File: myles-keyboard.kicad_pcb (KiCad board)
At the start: 2 copper layers, 208.8 x 114.3 mm, 52 parts, among them J1 TRRS, J2 OLED, SW00 Key, SW01 Key, SW02 Key, SW03 Key, SW04 Key, SW05 Key, SW10 Key, SW11 Key, SW12 Key, SW13 Key, SW14 Key, SW15 Key, SW16 Key, SW17 Key, SW18 Key, SW20 Key, SW21 Key, SW22 Key, SW23 Key, SW24 Key, SW25 Key, SW26 Key, SW27 Key, SW28 Key, SW30 Key, SW31 Key, SW32 Key, SW33 Key, SW34 Key, SW35 Key, SW36 Key, SW37 Key, SW38 Key, SW40 Key, SW41 Key, SW42 Key, SW43 Key, SW44 Key, SW45 Key, SW46 Key, SW47 Key, SW48 Key, U1 ProMicro

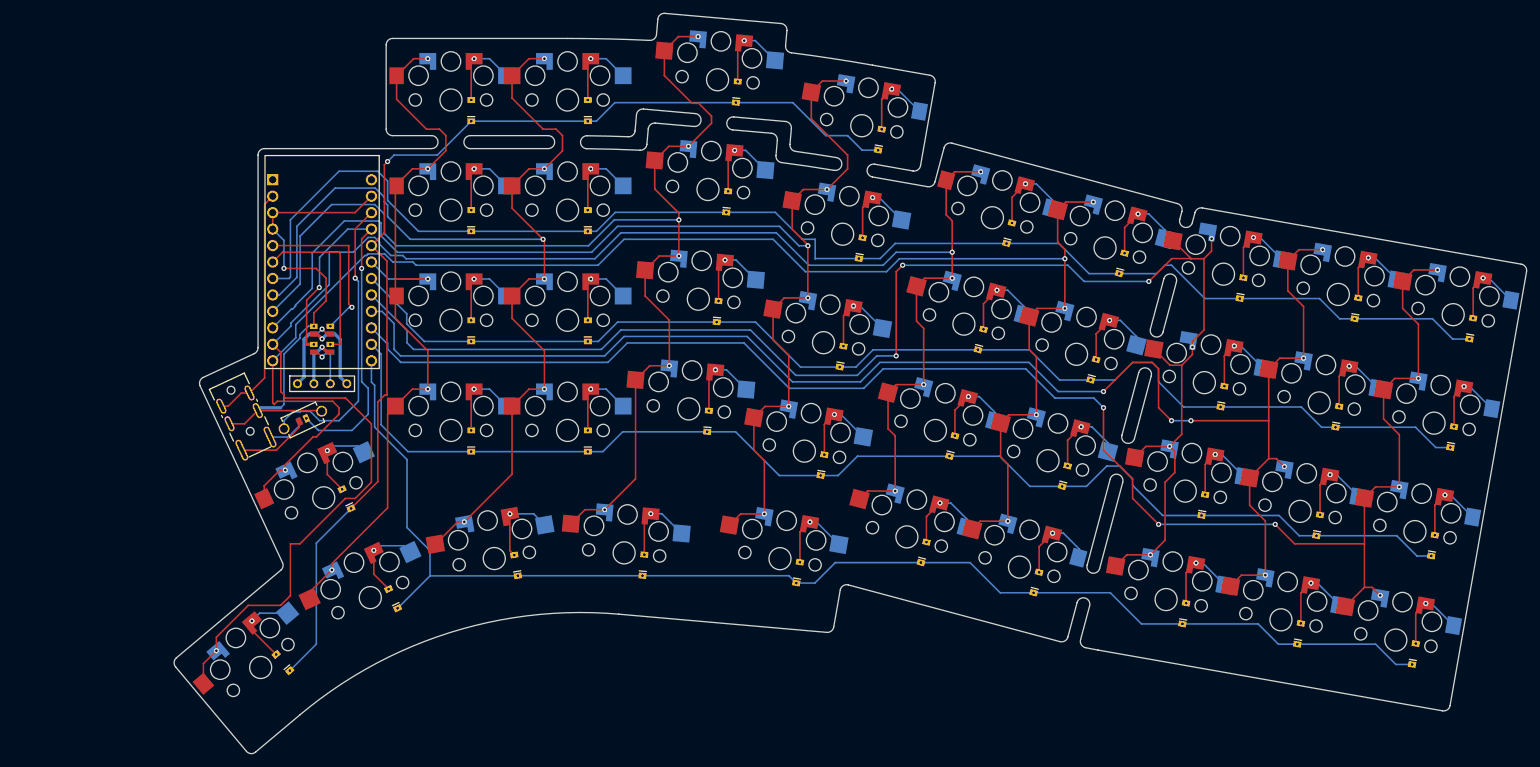
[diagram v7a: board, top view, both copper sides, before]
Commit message: tidy wiring
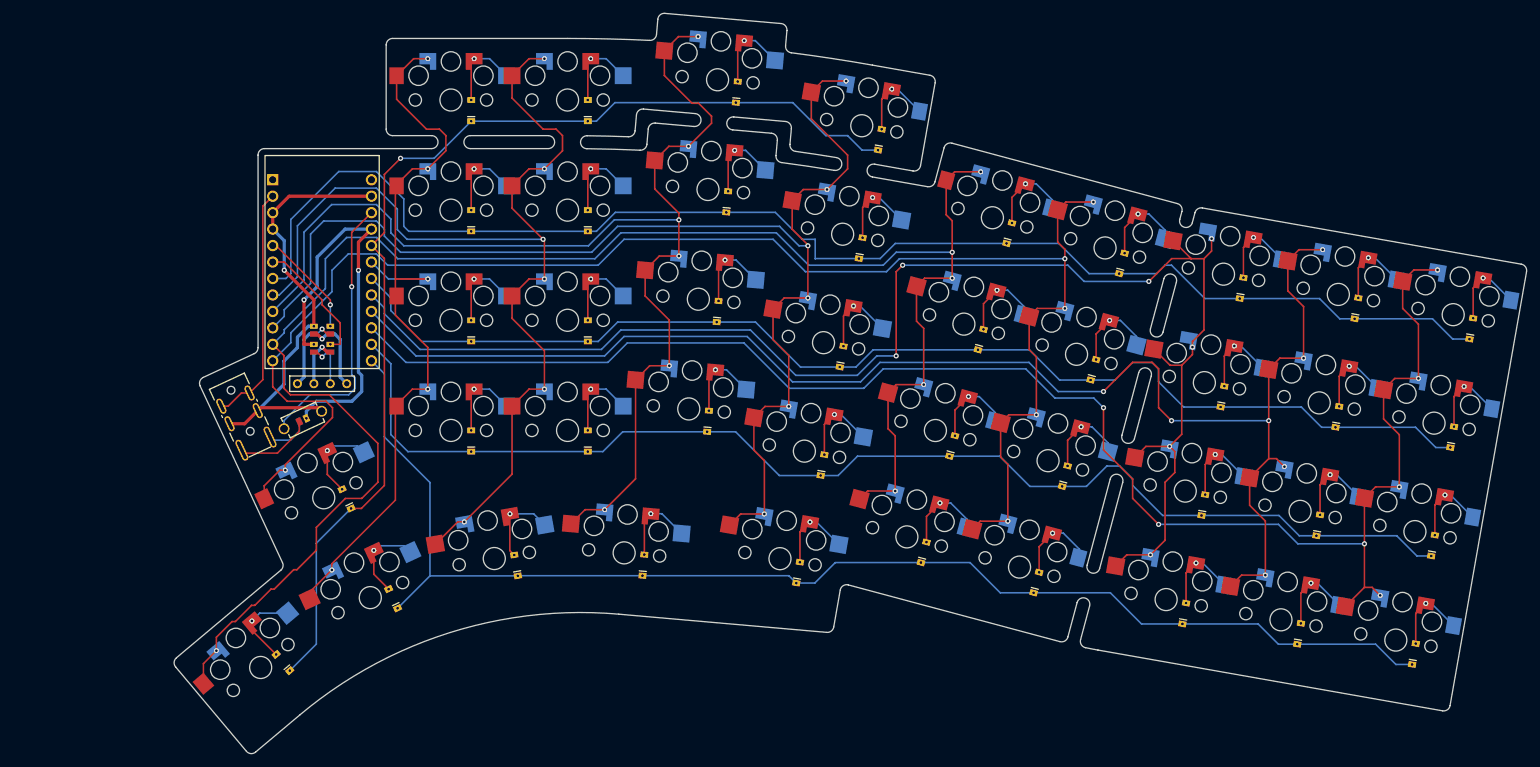
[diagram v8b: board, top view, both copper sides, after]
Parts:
- SW30: footprint myles-keyboard:Key -> myles-keyboard:KeyLeft
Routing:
- net SDA: track 26.0 -> 16.4 mm
- net SCL: track 26.7 -> 19.6 mm
- net GND: track 75.0 -> 69.0 mm
- net col4: track 271.3 -> 267.8 mm
- net VCC: track 66.2 -> 63.0 mm
- net RESET: track 45.5 -> 42.9 mm
- net col7: track 237.9 -> 235.6 mm
- net col5: track 243.6 -> 241.7 mm
- net col3: track 203.8 -> 205.1 mm
- net Net-(J1-Pad4): track 5.89 -> 6.77 mm
- net Net-(J1-Pad3): track 11.2 -> 11.9 mm
- net col8: track 256.1 -> 255.5 mm
- net col6: track 235.9 -> 235.3 mm
- net col2: track 184.9 -> 184.4 mm
